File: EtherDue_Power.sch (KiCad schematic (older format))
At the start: 47 parts, among them Q501 BC847BSMD, U203 LMV358IDGKR, U501 POWERJACK, U502 LM2734Y, U503 FDN340P, U504 FDN340P, U505 NCP1117ST33T3G

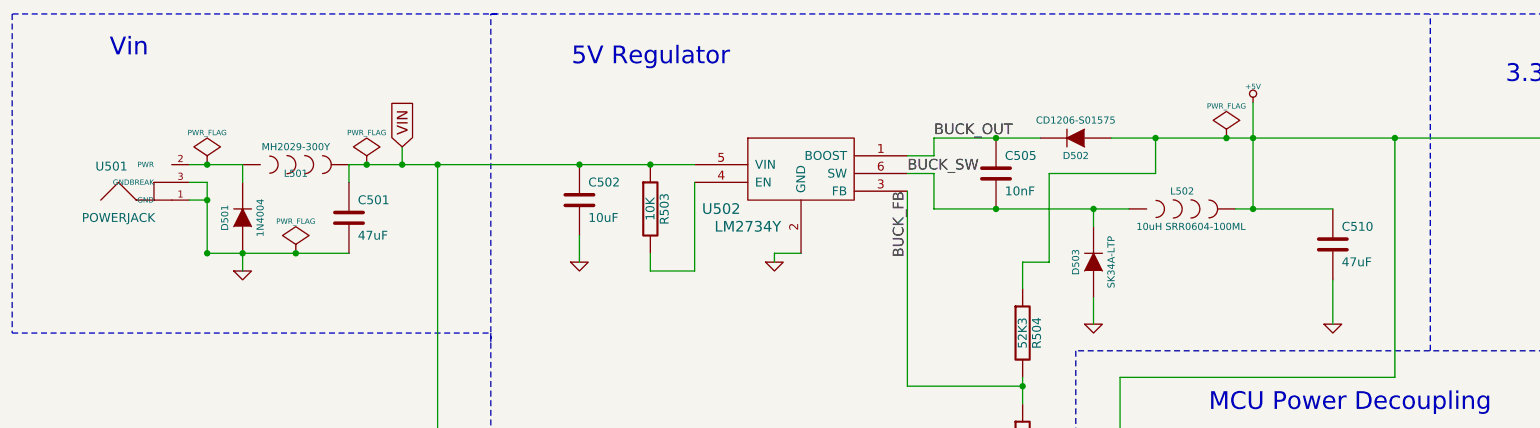
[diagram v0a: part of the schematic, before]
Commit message: Pre-autorouter hand routed traces
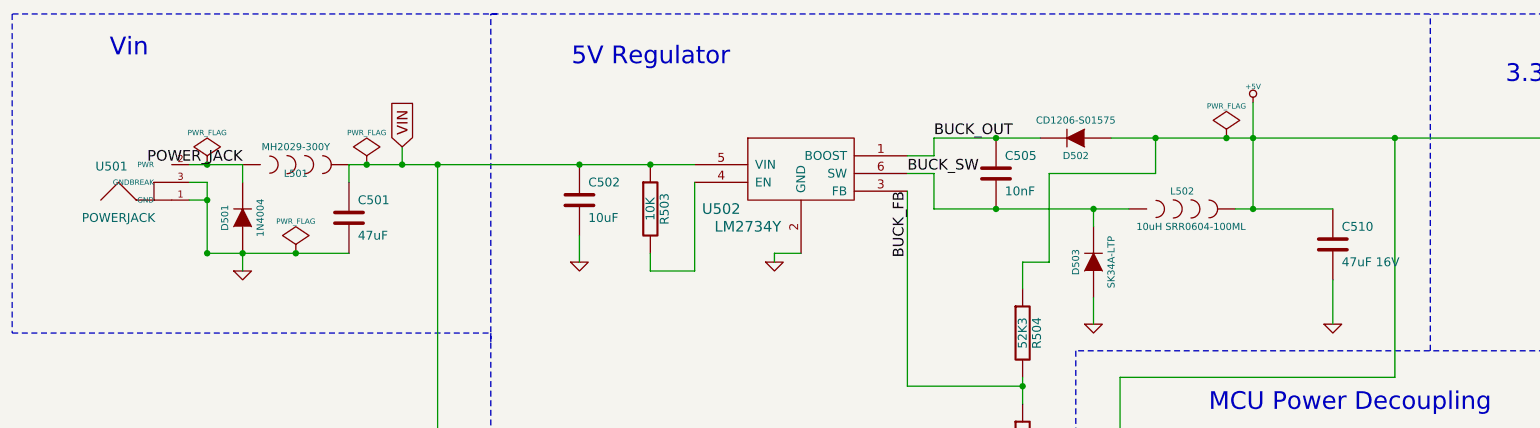
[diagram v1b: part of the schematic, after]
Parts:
- C510: value 47uF -> 47uF 16V
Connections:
- net POWER_JACK: now reaches D501.K, L501.1, U501.2 (PWR)
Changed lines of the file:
@@
-EESchema Schematic File Version 2  date Thu 06 Jun 2013 17:31:40 EST
+EESchema Schematic File Version 2  date Wed 19 Jun 2013 10:44:48 EST
 LIBS:freetronics_kicad_sch_lib
 LIBS:power
@@
 Sheet 5 6
 Title ""
-Date "6 jun 2013"
+Date "19 jun 2013"
 Rev ""
 Comp ""
@@
 P 8000 1850
 F 0 "C510" H 8050 1950 50  0000 L CNN
-F 1 "47uF" H 8050 1750 50  0000 L CNN
+F 1 "47uF 16V" H 8050 1750 50  0000 L CNN
 F 2 "" H 8000 1850 60  0001 C CNN
 F 3 "" H 8000 1850 60  0001 C CNN
@@
 	1    0    0    -1
 $EndComp
+Text Label 5600 1550 3    60   ~ 0
+BUCK_FB
+Text Label 5750 1250 0    60   ~ 0
+BUCK_OUT
+Text Label 5600 1450 0    60   ~ 0
+BUCK_SW
+Wire Wire Line
+	7150 6950 9100 6950
+Text Label 1850 1400 2    60   ~ 0
+POWER_JACK
 $Comp
 L PWR_FLAG #FLG078
@@
 $EndComp
 Connection ~ 2150 1900
-Text Label 5600 1550 3    60   ~ 0
-BUCK_FB
-Text Label 5750 1250 0    60   ~ 0
-BUCK_OUT
-Text Label 5600 1450 0    60   ~ 0
-BUCK_SW
-Wire Wire Line
-	7150 6950 9100 6950
 $EndSCHEMATC

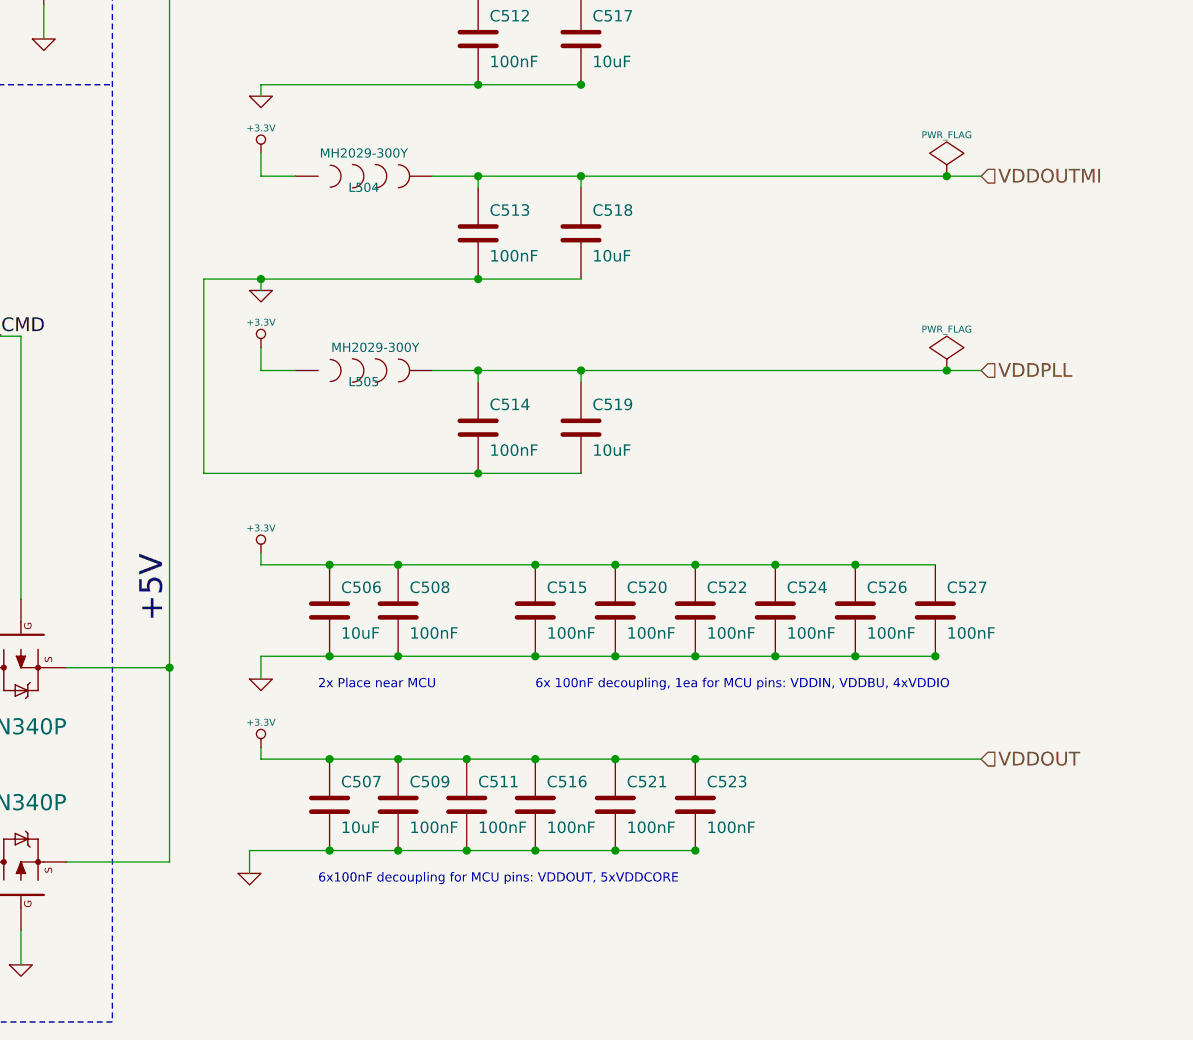
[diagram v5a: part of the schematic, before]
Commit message: Big power fixes: Fix major problem with VDDOUT/1.8V net, rearrange decoupling capacitors
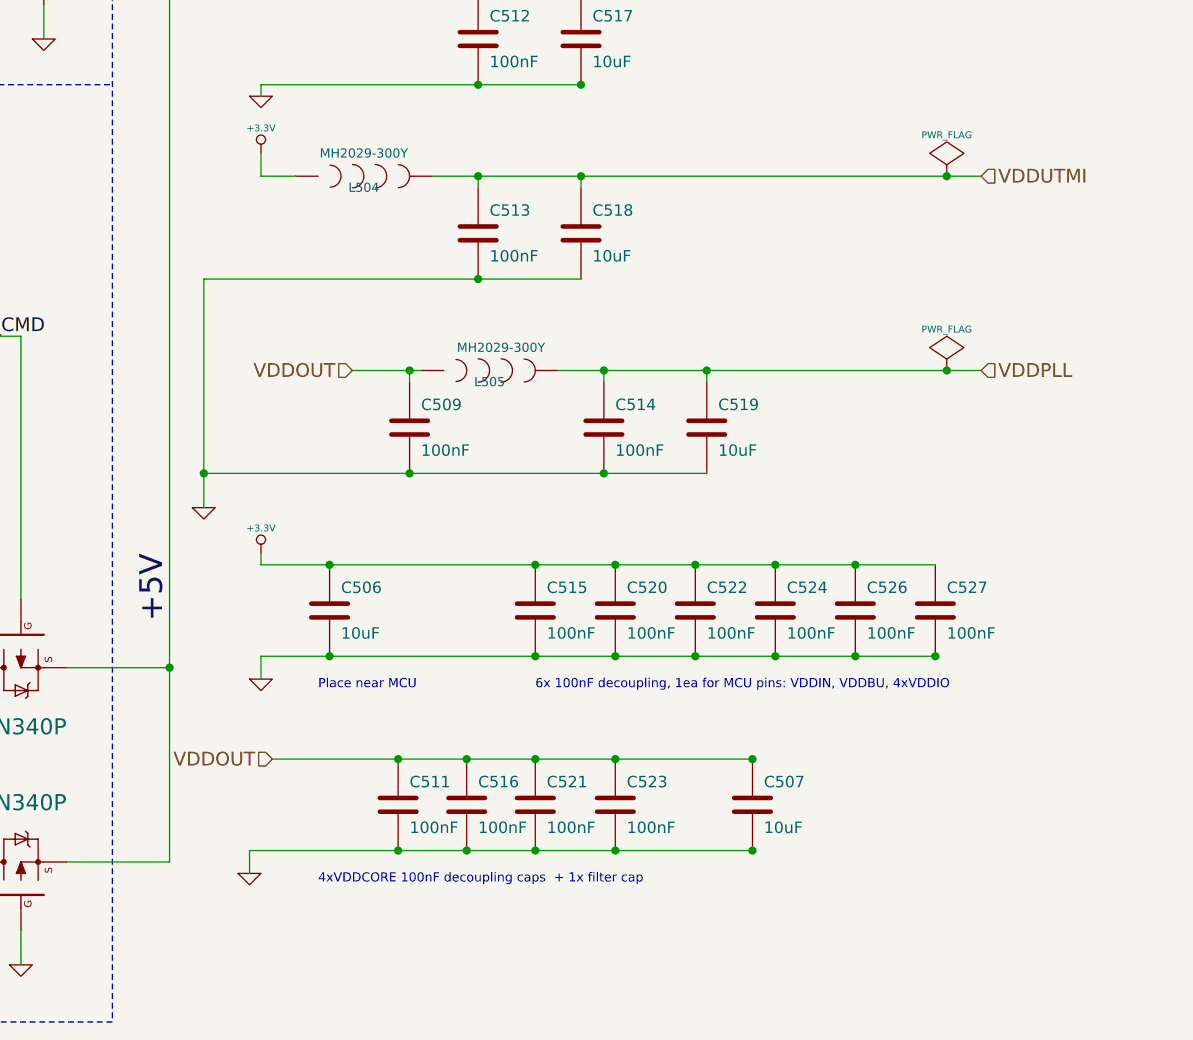
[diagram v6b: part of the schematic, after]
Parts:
- removed C508: 100nF, symbol C
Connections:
- net +3.3V: no longer C507.1, C509.1, C511.1, C516.1, C521.1, C523.1, L505.1
- net VDDOUTMI renamed VDDUTMI
- new net VDDOUT: C507.1, C509.1, C511.1, C516.1, C521.1, C523.1, L505.1
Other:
- note added: "4xVDDCORE 100nF decoupling caps + 1x filter cap\n"
- note added: "Place near MCU"
- note removed: "2x Place near MCU"
- note removed: "6x100nF decoupling for MCU pins: VDDOUT, 5xVDDCORE"
- moved on the sheet: C507, C509, C511, C514, C516, C519, C521, C523, L505

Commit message: Lots of minor cleanup - routing, silkscreen, component positions pre-v0.2 prototype
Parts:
- C501: value 47uF -> 47uF 25V
- C502: value 10uF -> 10uF 25V
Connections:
- net VIN: no longer C502.1
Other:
- moved on the sheet: C502
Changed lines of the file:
@@
 L GND #PWR073
 U 1 1 515CCC19
-P 3750 1950
-F 0 "#PWR073" H 3750 1950 30  0001 C CNN
-F 1 "GND" H 3750 1880 30  0001 C CNN
-F 2 "" H 3750 1950 60  0001 C CNN
-F 3 "" H 3750 1950 60  0001 C CNN
-	1    3750 1950
+P 3650 1950
+F 0 "#PWR073" H 3650 1950 30  0001 C CNN
+F 1 "GND" H 3650 1880 30  0001 C CNN
+F 2 "" H 3650 1950 60  0001 C CNN
+F 3 "" H 3650 1950 60  0001 C CNN
+	1    3650 1950
 	1    0    0    -1
 $EndComp
@@
 L C C502
 U 1 1 515CCC11
-P 3750 1600
-F 0 "C502" H 3800 1700 50  0000 L CNN
-F 1 "10uF" H 3800 1500 50  0000 L CNN
-F 2 "" H 3750 1600 60  0001 C CNN
-F 3 "" H 3750 1600 60  0001 C CNN
-	1    3750 1600
+P 3650 1600
+F 0 "C502" H 3700 1700 50  0000 L CNN
+F 1 "10uF 25V" H 3700 1500 50  0000 L CNN
+F 2 "" H 3650 1600 60  0001 C CNN
+F 3 "" H 3650 1600 60  0001 C CNN
+	1    3650 1600
 	1    0    0    -1
 $EndComp
@@
 P 2450 1700
 F 0 "C501" H 2500 1800 50  0000 L CNN
-F 1 "47uF" H 2500 1600 50  0000 L CNN
+F 1 "47uF 25V" H 2500 1600 50  0000 L CNN
 F 2 "" H 2450 1700 60  0001 C CNN
 F 3 "" H 2450 1700 60  0001 C CNN
@@
 	5750 1350 5600 1350
 Wire Wire Line
-	3750 1800 3750 1950
+	3650 1800 3650 1950
 Connection ~ 4150 1400
 Wire Wire Line

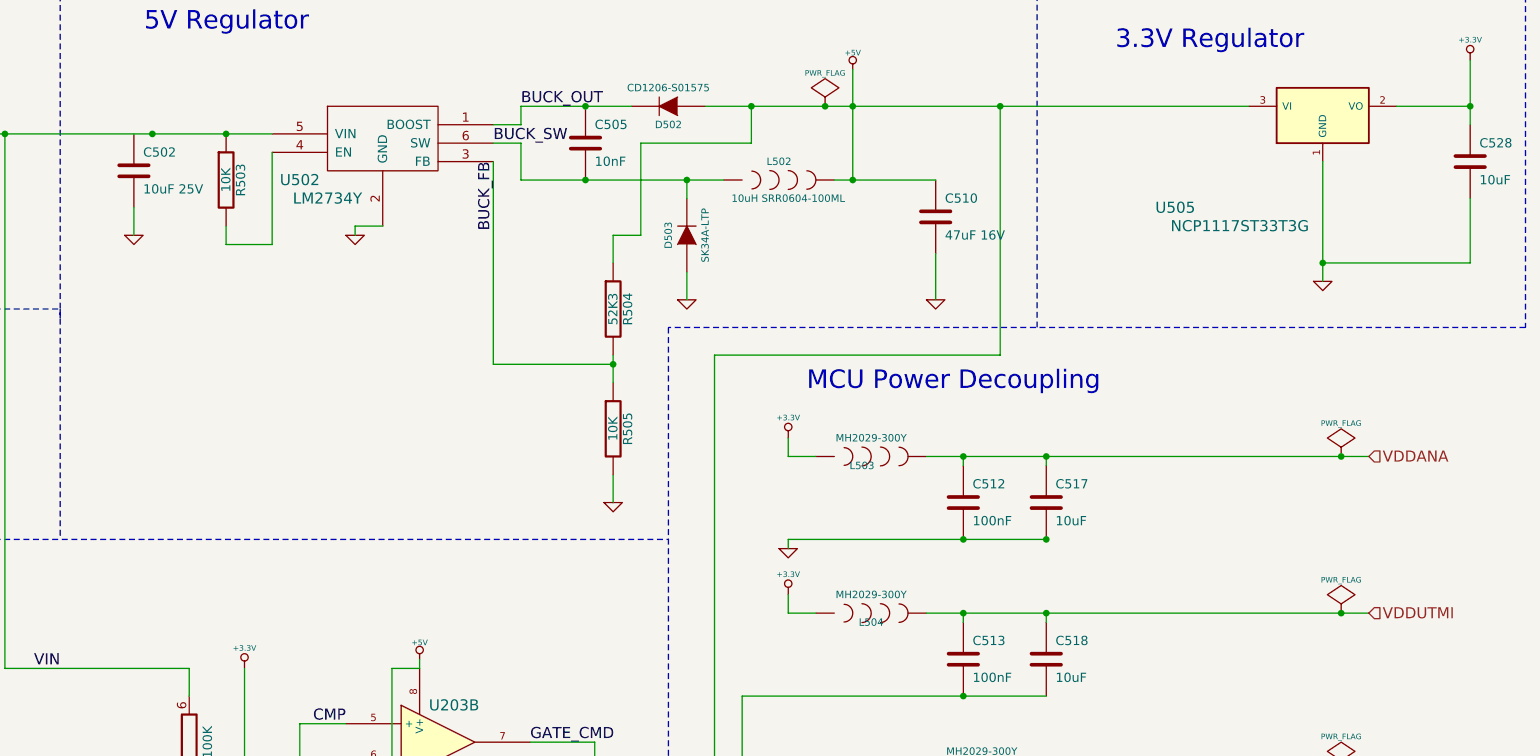
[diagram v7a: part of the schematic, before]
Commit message: Fix footprint association on resistor network for RJ45 connection
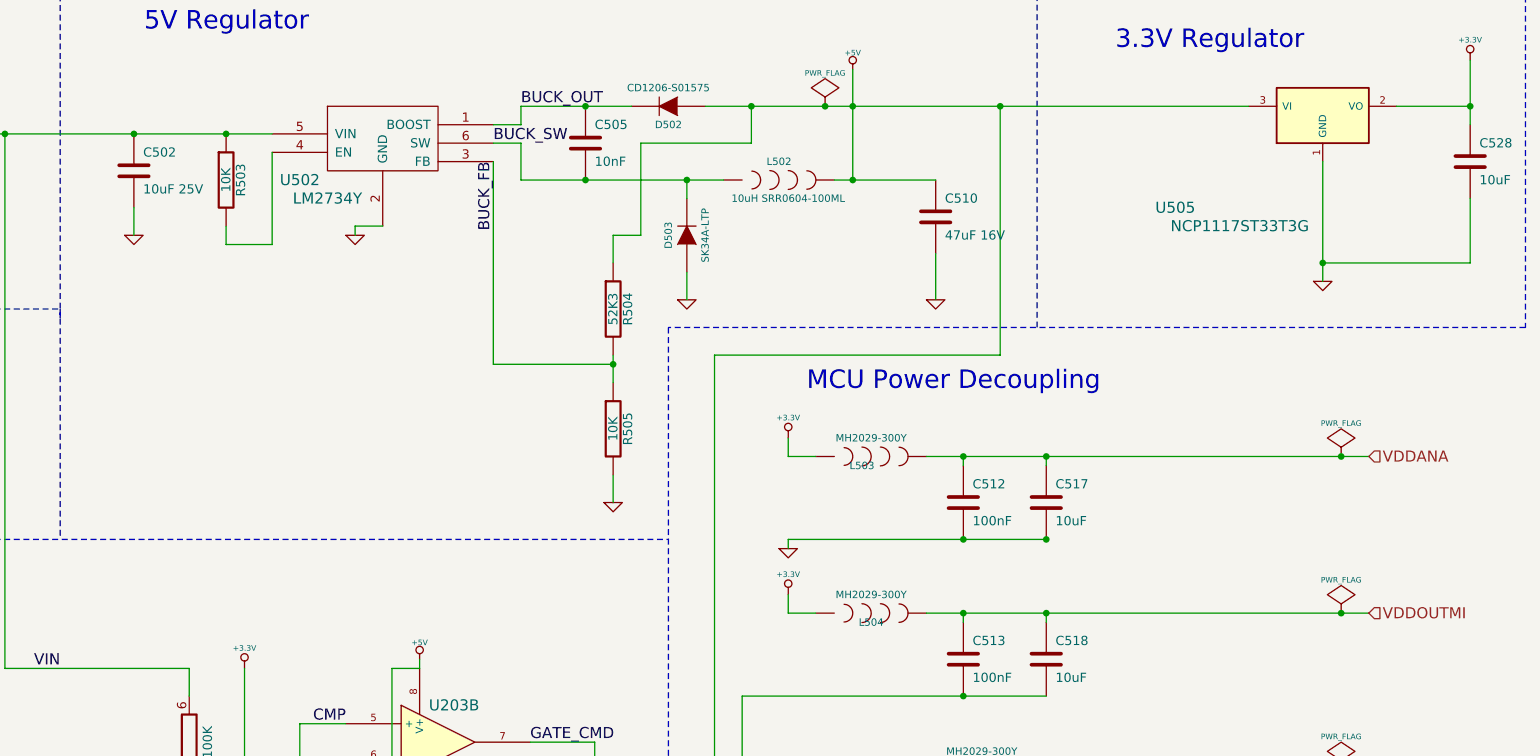
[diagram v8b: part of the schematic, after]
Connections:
- net VIN: now also C502.1
- net VDDUTMI renamed VDDOUTMI
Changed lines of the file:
@@
 LIBS:valves
 LIBS:EtherDue-cache
-EELAYER 24 0
+EELAYER 27 0
 EELAYER END
 $Descr A4 11693 8268
@@
 Sheet 5 7
 Title ""
-Date "4 jul 2013"
+Date "20 nov 2013"
 Rev ""
 Comp ""
@@
 $EndComp
 Text HLabel 10350 4000 2    60   Input ~ 0
-VDDUTMI
+VDDOUTMI
 $Comp
 L GND #PWR056
@@
 	2750 1300 2750 1400
 Connection ~ 2750 1400
-Connection ~ 3750 1400
+Connection ~ 3650 1400
 Wire Wire Line
 	4400 1500 4400 2000
